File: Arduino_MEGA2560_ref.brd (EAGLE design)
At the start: 75.2 x 77.1 mm, 75 parts, among them IC1 7805DT, IC2 7805DT, T1 PHT8N06LTSOT223, T2 PHT8N06LTSOT223, T3 PHT8N06LTSOT223, T4 PHT8N06LTSOT223, T5 PHT8N06LTSOT223, T6 PHT8N06LTSOT223, X1 MKDSN1,5/2-5,08, X2 MKDSN1,5/2-5,08, X3 MKDSN1,5/2-5,08, X4 MKDSN1,5/2-5,08, X5 MKDSN1,5/2-5,08, X6 MKDSN1,5/2-5,08, X7 5566-4, X9 MKDSN1,5/2-5,08

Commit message: doing factory
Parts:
- removed C7, C8: 1uF, resistor:C0805
- removed T1, T3, T4, T5, T6: PHT8N06LTSOT223, NFET_transistors:SOT223
- removed X10, X11, X12, X13, X14: (no value), con-phoenix-254:2POL254
- added Q1, Q11, Q13, Q3, Q5, Q7, Q9: IRLML2502, NFET_transistors:SOT23
- added Q10, Q14, Q2, Q4, Q6, Q8: PF610BL, NFET_transistors:SOT223
- added R22: 0, resistor:M0805
- added X15, X16: 1751251, con-phoenix-350:1751251
- added X17: 1751264, con-phoenix-350:1751264
- Q12: value PHT8N06LTSOT223 -> PF610BL
- R15: value 10 -> 1K
- R16: value 1K -> 0
- X8: value (none) -> 1751248; device con-phoenix-254:2POL254 -> con-phoenix-350:1751248
- moved X8 101.9 mm to (116.2, 44.5), turned to 90 degrees
- moved R16 36.3 mm to (108.6, 39.2), turned to 270 degrees
- moved R20 29.6 mm to (91.7, 64.6), turned to 270 degrees
- moved D1 28.3 mm to (45.1, -13.3), flipped to the bottom, turned to 180 degrees
- moved C3 23.5 mm to (28.7, 20.2), turned to 0 degrees
- moved D2 22.8 mm to (55.9, -13.3), flipped to the bottom, turned to 180 degrees
- moved IC1 22.0 mm to (22.9, 14.4)
- moved R14 21.4 mm to (31.1, 39.1), turned to 90 degrees
- moved X1 19.7 mm to (45.1, -19.7)
- moved R13 18.8 mm to (27.7, 39.1), turned to 90 degrees
- moved R2 17.5 mm to (48.1, -8.05), turned to 90 degrees
- moved D3 16.7 mm to (66.7, -13.3), flipped to the bottom, turned to 180 degrees
- moved X6 15.2 mm to (99.1, -19.7)
- moved X2 14.6 mm to (55.9, -19.7)
- moved X7 14.1 mm to (18.4, -5.08)
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- renumbered T2 to Q12
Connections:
- net +5V: now also R15.1, X15.2, X16.2; no longer X11.1, X13.2
- net GND: now also Q1.S, Q10.S, Q11.S, Q2.S, Q3.S, Q4.S, Q5.S, Q6.S, Q7.S, Q8.S, Q9.S, R16.2, R22.2, X15.1, X16.3, X17.1, X17.2; no longer T1.S, T3.S, T4.S, T5.S, T6.S, X11.2, X13.1, X14.1, X8.1
- net GNDA: now also Q13.S, Q14.S, R22.1; no longer C7.2, C8.2
- net N$1: now also Q11.G, Q12.G; no longer T1.G
- net N$10: now also Q1.D, Q2.D, Q2.D_TAB; no longer T5.D, T5.D_TAB
- net N$11: now also Q5.G, Q6.G; no longer T6.G
- net N$12: now also Q5.D, Q6.D, Q6.D_TAB; no longer T6.D, T6.D_TAB
- net N$14: now also Q13.D, Q14.D, Q14.D_TAB; no longer R16.2
- net N$17: no longer C8.1
- net N$18: now also X8.1; no longer X10.1
- net N$2: now also Q10.G, Q9.G; no longer Q12.G
- net N$21: now also Q13.G, Q14.G; no longer C7.1, R15.1
- net N$22: now also X8.2; no longer X10.2
- net N$3: now also Q3.G, Q4.G; no longer T4.G
- net N$4: now also Q11.D, Q12.D, Q12.D_TAB; no longer T1.D, T1.D_TAB
- net N$5: now also Q7.G, Q8.G; no longer T3.G
- net N$6: now also Q10.D, Q10.D_TAB, Q9.D; no longer Q12.D, Q12.D_TAB
- net N$7: now also Q7.D, Q8.D, Q8.D_TAB; no longer T3.D, T3.D_TAB
- net N$8: now also Q3.D, Q4.D, Q4.D_TAB; no longer T4.D, T4.D_TAB
- net N$9: now also Q1.G, Q2.G; no longer T5.G
- net PB4: now also X15.3; no longer X12.2
- net PB6: now also X17.3; no longer X14.2
- net PB7: now also X17.4; no longer X8.2
- net PH6: now also X16.1; no longer X12.1
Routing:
- net +5V: track 12.2 -> 217.9 mm
- net +12V: track 44.0 -> 171.3 mm
- net N$18: track 0.00 -> 58.8 mm
- net PH3: track 0.00 -> 47.8 mm
- net PH6: track 0.00 -> 39.4 mm
- net PB7: track 0.00 -> 38.1 mm
- net PB6: track 0.00 -> 36.3 mm
- net +24V: track 0.00 -> 28.5 mm
- net N$8: track 0.74 -> 25.5 mm
- net PB4: track 0.00 -> 23.5 mm
- net N$12: track 2.86 -> 25.8 mm
- net N$6: track 3.43 -> 26.1 mm
- net N$7: track 5.16 -> 26.1 mm
- net N$4: track 7.51 -> 26.7 mm
- net N$10: track 1.57 -> 19.7 mm
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- added copper zone on layer 16, net GNDA
- added copper zone on layer 16, net N$19
- removed copper zone on layer 1, net +12V
- removed copper zone on layer 1, net +24V
- removed copper zone on layer 1, net +5V
- removed copper zone on layer 1, net +5V_1
- removed copper zone on layer 1, net ADC0
- removed copper zone on layer 1, net ADC1
- removed copper zone on layer 1, net ADC14
- removed copper zone on layer 1, net ADC15
- removed copper zone on layer 1, net ADC5
- removed copper zone on layer 1, net ADC8
- removed copper zone on layer 1, net N$1
- removed copper zone on layer 1, net N$10
- removed copper zone on layer 1, net N$11
- removed copper zone on layer 1, net N$12
- removed copper zone on layer 1, net N$13
- removed copper zone on layer 1, net N$14
- removed copper zone on layer 1, net N$17
- removed copper zone on layer 1, net N$18
- removed copper zone on layer 1, net N$2
- removed copper zone on layer 1, net N$20
- removed copper zone on layer 1, net N$21
- removed copper zone on layer 1, net N$22
- removed copper zone on layer 1, net N$3
- removed copper zone on layer 1, net N$4
- removed copper zone on layer 1, net N$5
- removed copper zone on layer 1, net N$6
- removed copper zone on layer 1, net N$7
- removed copper zone on layer 1, net N$8
- removed copper zone on layer 1, net N$9
- removed copper zone on layer 1, net PB4
- removed copper zone on layer 1, net PB6
- removed copper zone on layer 1, net PB7
- removed copper zone on layer 1, net PH3
- removed copper zone on layer 1, net PH6
- removed copper zone on layer 1, net TXD1/INT3
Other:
- board size 75.2 x 77.1 mm -> 66.7 x 104.8 mm

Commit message: doiing CAM
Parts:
- removed ICSP: ICSP, pinhead:2X03
- added TP1: PTR1TP20SQ, testpad:TP20SQ
- added X10: MKDSN1,5/2-5,08, con-phoenix-508:MKDSN1,5/2-5,08
- moved R21 12.0 mm to (106.7, 42.3), turned to 270 degrees
- moved X8 8.26 mm to (116.2, 36.2)
- moved R16 7.67 mm to (108.0, 31.6)
- moved R22 7.64 mm to (104.2, 31.6)
- moved C4 6.81 mm to (102.2, 49.8), turned to 270 degrees
- moved L3 2.95 mm to (106.7, 48.7), turned to 270 degrees
- moved C5 1.91 mm to (109.2, 61.2)
- moved R13 1.09 mm to (28.8, 39.1)
- moved R14 0.64 mm to (31.8, 39.1)
- moved Q5 0.20 mm to (97.8, -3.38)
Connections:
- net +24V: now also X10.1
- net GND: now also X16.1; no longer X16.3
- net GNDA: now also X10.2
- net N$21: now also TP1.TP
- net PH6: now also X16.3; no longer X16.1
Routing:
- net +24V: track 28.5 -> 45.5 mm
- net N$22: track 4.62 -> 13.0 mm
- net N$18: track 58.8 -> 67.0 mm
- net PH6: track 39.4 -> 32.4 mm
- net N$21: track 10.3 -> 13.6 mm
- net N$20: track 9.34 -> 7.49 mm
- net +5V: track 217.9 -> 216.6 mm
- net PB7: track 38.1 -> 37.0 mm
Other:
- board size 66.7 x 104.8 mm -> 111.8 x 102.9 mm
- board text added: "+12V"
- board text added: "24V"
- board text added: "5V"
- board text added: "Feedback"
- board text added: "From Servo Motors"
- board text added: "GND"
- board text added: "PWM"

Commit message: done factory
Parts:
- moved C5 48.7 mm to (76.4, 97.2), turned to 180 degrees
- moved C6 33.8 mm to (72.1, 94.7)
- moved L3 33.8 mm to (85.1, 74.8)
- moved R21 33.8 mm to (85.1, 68.3)
- moved X9 33.8 mm to (94.6, 85.7)
- moved X8 33.4 mm to (95.2, 62.2)
- moved X10 33.3 mm to (94.6, 74.3)
- moved TP1 32.1 mm to (83.7, 81.4)
- moved L4 31.9 mm to (88.3, 81.9)
- moved Q13 31.9 mm to (87.0, 87.6)
- moved R16 31.9 mm to (89.6, 57.6)
- moved R22 31.5 mm to (86.4, 57.7)
- moved Q14 31.5 mm to (80.6, 86.4)
- moved IC2 31.4 mm to (84.5, 95.2)
- moved R20 31.2 mm to (74.6, 90.7)
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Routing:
- net +12V: track 171.3 -> 165.0 mm
- net PB6: track 36.5 -> 30.8 mm
- net PB7: track 37.0 -> 31.3 mm
- net N$18: track 67.0 -> 61.9 mm
- net +5V: track 216.6 -> 213.3 mm
- net N$20: track 7.49 -> 10.7 mm
- net N$14: track 17.9 -> 15.3 mm
- net +5V_1: track 12.5 -> 10.3 mm
- net PH6: track 32.4 -> 34.3 mm
- net PB4: track 23.5 -> 25.4 mm
- net N$21: track 13.6 -> 12.3 mm
- net N$13: track 3.46 -> 2.82 mm
- net N$22: track 13.0 -> 13.7 mm
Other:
- board size 111.8 x 102.9 mm -> 100 x 100 mm

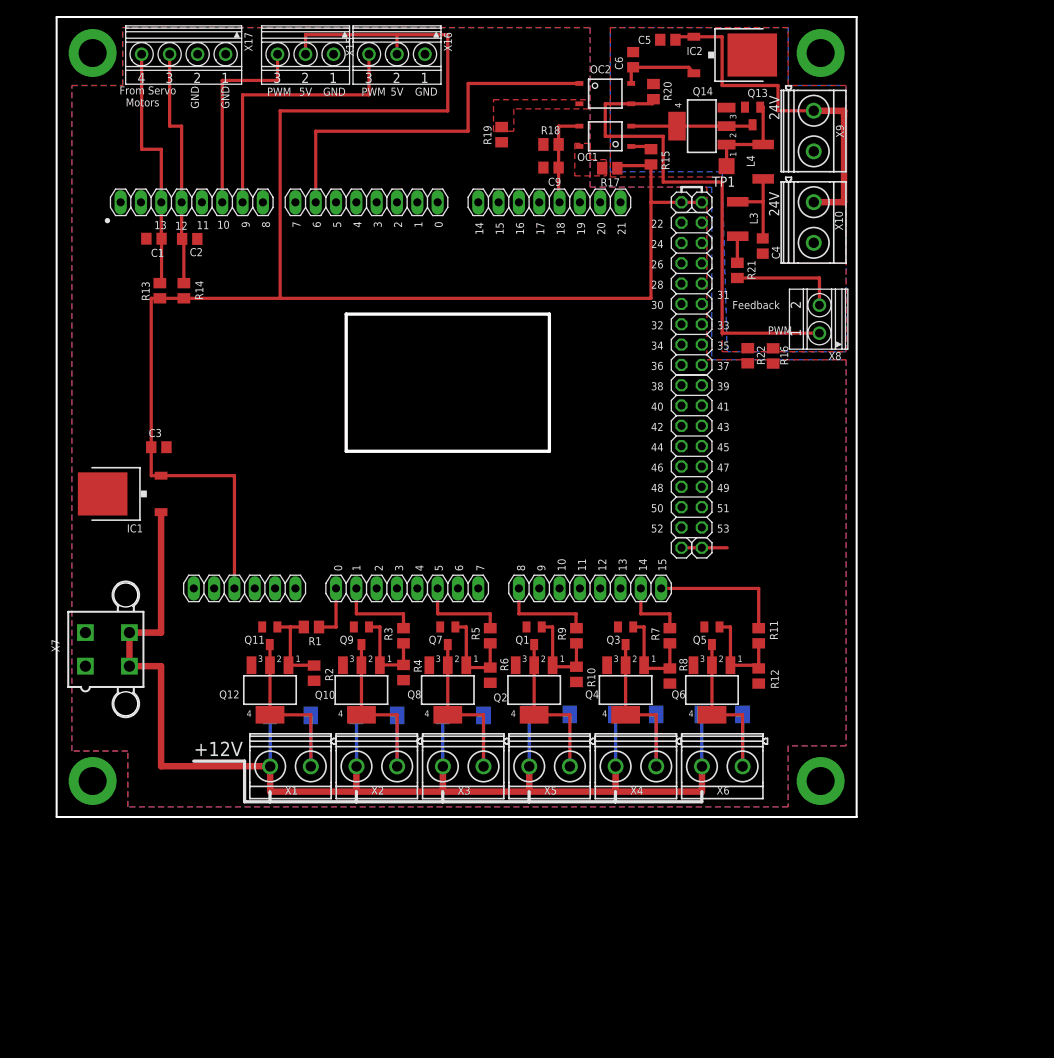
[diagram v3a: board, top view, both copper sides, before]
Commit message: Added new Valves controls
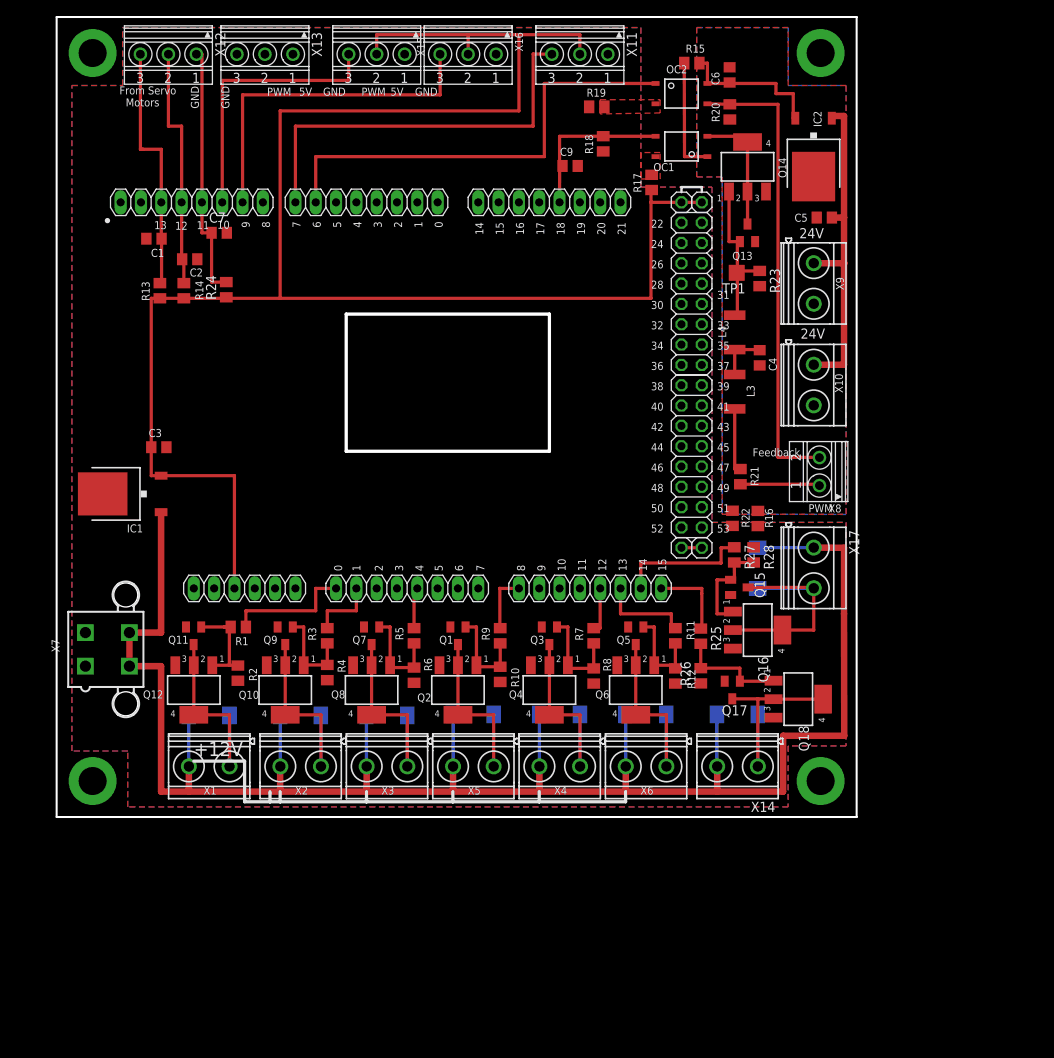
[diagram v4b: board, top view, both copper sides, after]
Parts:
- added C7: 0.1uF, resistor:C0805
- added D7, D8: (no value), diode:DO214AA
- added Q15, Q17: IRLML2502, NFET_transistors:SOT23
- added Q16, Q18: PF610BL, NFET_transistors:SOT223
- added R23, R24, R26, R28: 1K, resistor:M0805
- added R25, R27: 10, resistor:M0805
- added X11, X12, X13: 1751251, con-phoenix-350:1751251
- added X14: MKDSN1,5/2-5,08, con-phoenix-508:MKDSN1,5/2-5,08
- X17: value 1751264 -> MKDSN1,5/2-5,08; device con-phoenix-350:1751264 -> con-phoenix-508:MKDSN1,5/2-5,08
- moved X17 101.6 mm to (94.6, 31.1), turned to 270 degrees
- moved C5 29.6 mm to (96.0, 74.9)
- moved R21 25.8 mm to (85.5, 42.5)
- moved L4 21.6 mm to (84.8, 60.6)
- moved L3 21.6 mm to (84.8, 53.2)
- moved R22 20.4 mm to (84.5, 37.3)
- moved R16 20.4 mm to (87.7, 37.3)
- moved X10 20.3 mm to (94.6, 54.0)
- moved X8 19.0 mm to (95.2, 43.2)
- moved X9 19.0 mm to (94.6, 66.7)
- moved IC2 16.3 mm to (94.6, 82.5), turned to 180 degrees
- moved Q13 14.6 mm to (86.4, 73.0), turned to 0 degrees
- moved C4 14.0 mm to (87.9, 57.4)
- moved TP1 13.4 mm to (85.0, 68.0)
- moved R15 12.8 mm to (79.4, 94.2), turned to 180 degrees
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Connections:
- removed net PH5: PWMH.1
- new net N$24: Q17.G, Q18.G, R25.2, R26.2
- new net N$25: D7.A, Q17.D, Q18.D, Q18.D_TAB, X14.1
- new net N$26: Q15.G, Q16.G, R27.2, R28.2
- new net N$27: D8.A, Q15.D, Q16.D, Q16.D_TAB, X17.2
- net +12V: now also D7.C, D8.C, X14.2, X17.1
- net +5V: now also R24.1, X11.2; no longer R15.1
- net +5V_1: now also R15.1
- net ADC12: now also R7.1
- net ADC13: now also R11.1
- net ADC14: now also R27.1; no longer R7.1
- net ADC15: now also R25.1; no longer R11.1
- net ADC4: now also R5.1
- net ADC5: no longer R5.1
- net GND: now also C7.2, Q15.S, Q16.S, Q17.S, Q18.S, R26.1, R28.1, X11.1, X13.1, X13.2, X13.3; no longer X17.1, X17.2
- net GNDA: now also R23.2
- net N$18: now also X8.2; no longer X8.1
- net N$21: now also R23.1
- net N$22: now also X8.1; no longer X8.2
- net PB5: now also C7.1, R24.2, X12.1
- net PB6: now also X12.2; no longer X17.3
- net PB7: now also X12.3; no longer X17.4
- net PH4: now also X11.3
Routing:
- net +12V: track 165.0 -> 236.9 mm
- net PH4: track 0.00 -> 50.6 mm
- net N$27: track 0.00 -> 33.1 mm
- net PB5: track 0.00 -> 32.2 mm
- net N$25: track 0.00 -> 26.4 mm
- net N$26: track 0.00 -> 14.4 mm
- net N$24: track 0.00 -> 13.8 mm
- net ADC13: track 0.00 -> 11.8 mm
- net N$13: track 2.82 -> 14.5 mm
- net ADC5: track 11.5 -> 0.00 mm
- net +5V: track 213.3 -> 224.6 mm
- net PH3: track 47.8 -> 57.3 mm
- net ADC0: track 6.95 -> 16.1 mm
- net PB4: track 25.4 -> 34.3 mm
- net PH6: track 34.3 -> 43.2 mm
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
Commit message: Done new version - added new valves
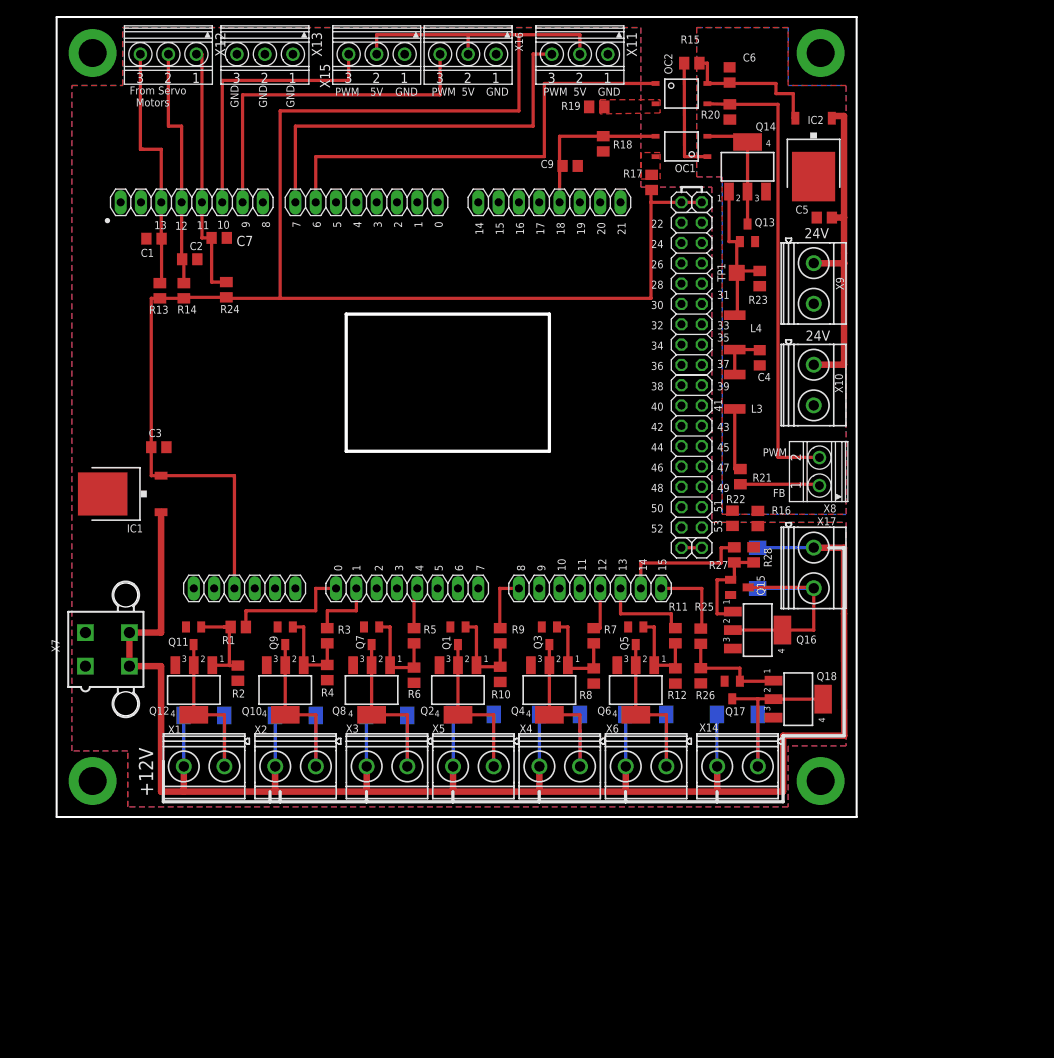
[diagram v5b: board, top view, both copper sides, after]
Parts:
- X1, X10, X14, X2, X3, X4, X5, X6, X9: value MKDSN1,5/2-5,08 -> MKDSN
- moved C7 0.64 mm to (20.3, 72.4)
- moved D1 0.64 mm to (18.4, 12.7)
- moved D2 0.64 mm to (29.8, 12.7)
- moved X1 0.64 mm to (18.4, 6.35)
- moved X2 0.64 mm to (29.8, 6.35)
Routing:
- net +24V: track 45.9 -> 42.0 mm
- net N$21: track 19.9 -> 20.7 mm
- net N$4: track 26.1 -> 25.5 mm
- net N$6: track 26.1 -> 25.4 mm
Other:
- board text added: "FB"
- board text removed: "Feedback"
